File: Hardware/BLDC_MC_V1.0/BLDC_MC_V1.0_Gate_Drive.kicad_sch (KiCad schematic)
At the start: 19 parts, among them U6 DRV8353HRTAR

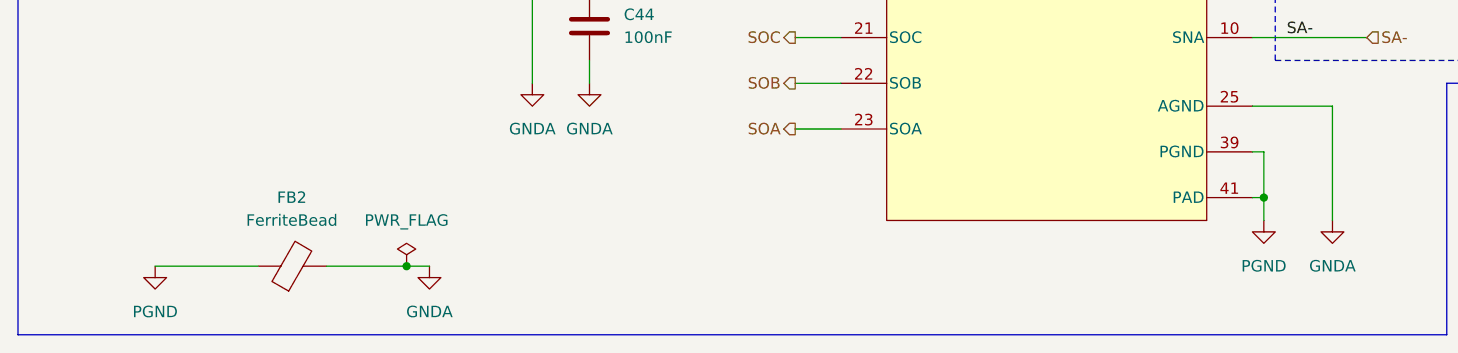
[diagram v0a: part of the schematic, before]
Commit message: Routing Power plans and change the power connedtors
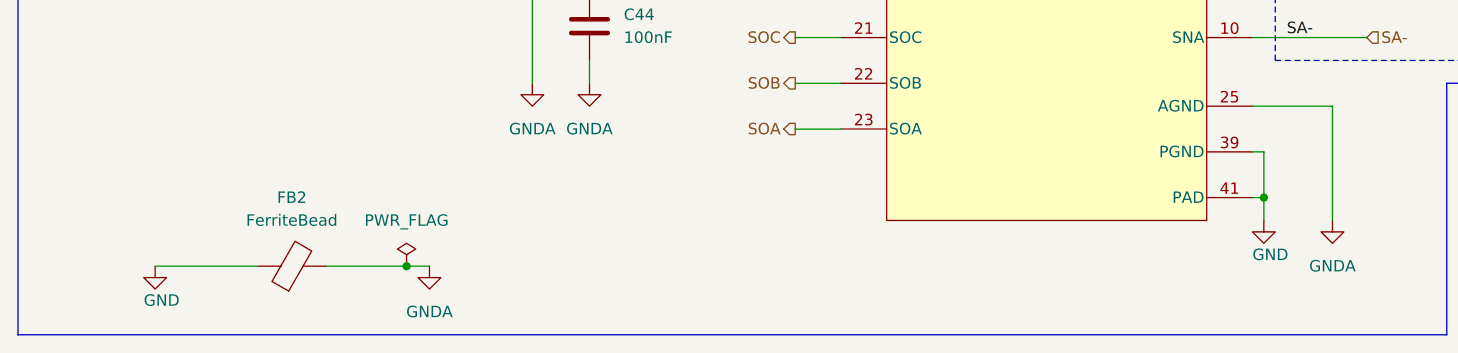
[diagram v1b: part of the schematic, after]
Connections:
- net PGND is gone; now on net GND: FB2.1, U6.39 (PGND), U6.41 (PAD)
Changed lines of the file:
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@@
 		(in_pos_files yes)
 		(dnp no)
-		(fields_autoplaced yes)
 		(property "Reference" "#PWR058"
 			(at 153.67 184.15 0)
@@
 			)
 		)
-		(property "Value" "PGND"
-			(at 153.67 182.88 0)
-			(show_name no)
-			(do_not_autoplace no)
-			(effects
-				(font
-					(size 1.27 1.27)
-				)
+		(property "Value" "GND"
+			(at 152.4 181.61 0)
+			(show_name no)
+			(do_not_autoplace no)
+			(effects
+				(font
+					(size 1.27 1.27)
+				)
+				(justify left)
 			)
 		)
@@
 		(in_pos_files yes)
 		(dnp no)
-		(fields_autoplaced yes)
 		(property "Reference" "#PWR0156"
 			(at 30.48 189.23 0)
@@
 			)
 		)
-		(property "Value" "PGND"
-			(at 30.48 187.96 0)
-			(show_name no)
-			(do_not_autoplace no)
-			(effects
-				(font
-					(size 1.27 1.27)
-				)
-			)
-		)
+		(property "Value" "GND"
+			(at 29.21 186.69 0)
+			(show_name no)
+			(do_not_autoplace no)
+			(effects
+				(font
+					(size 1.27 1.27)
+				)
+				(justify left)
+			)
+		)
